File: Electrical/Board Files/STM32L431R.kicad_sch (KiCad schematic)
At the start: 11 parts

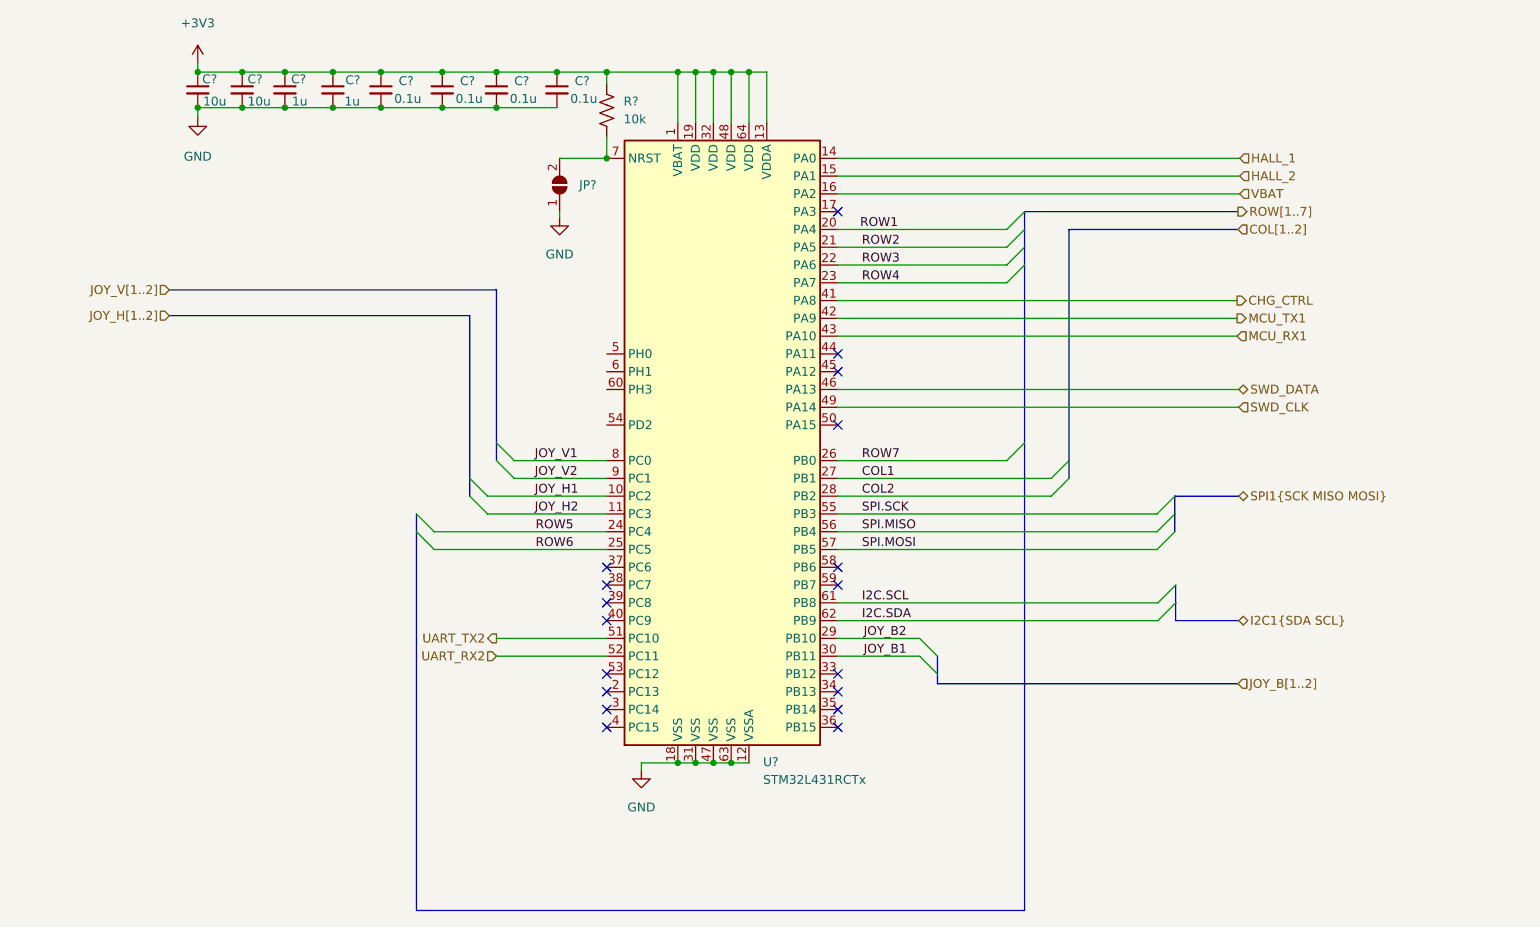
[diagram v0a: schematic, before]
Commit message: Added buzz and vibe, moved SPI, added 2 LEDs
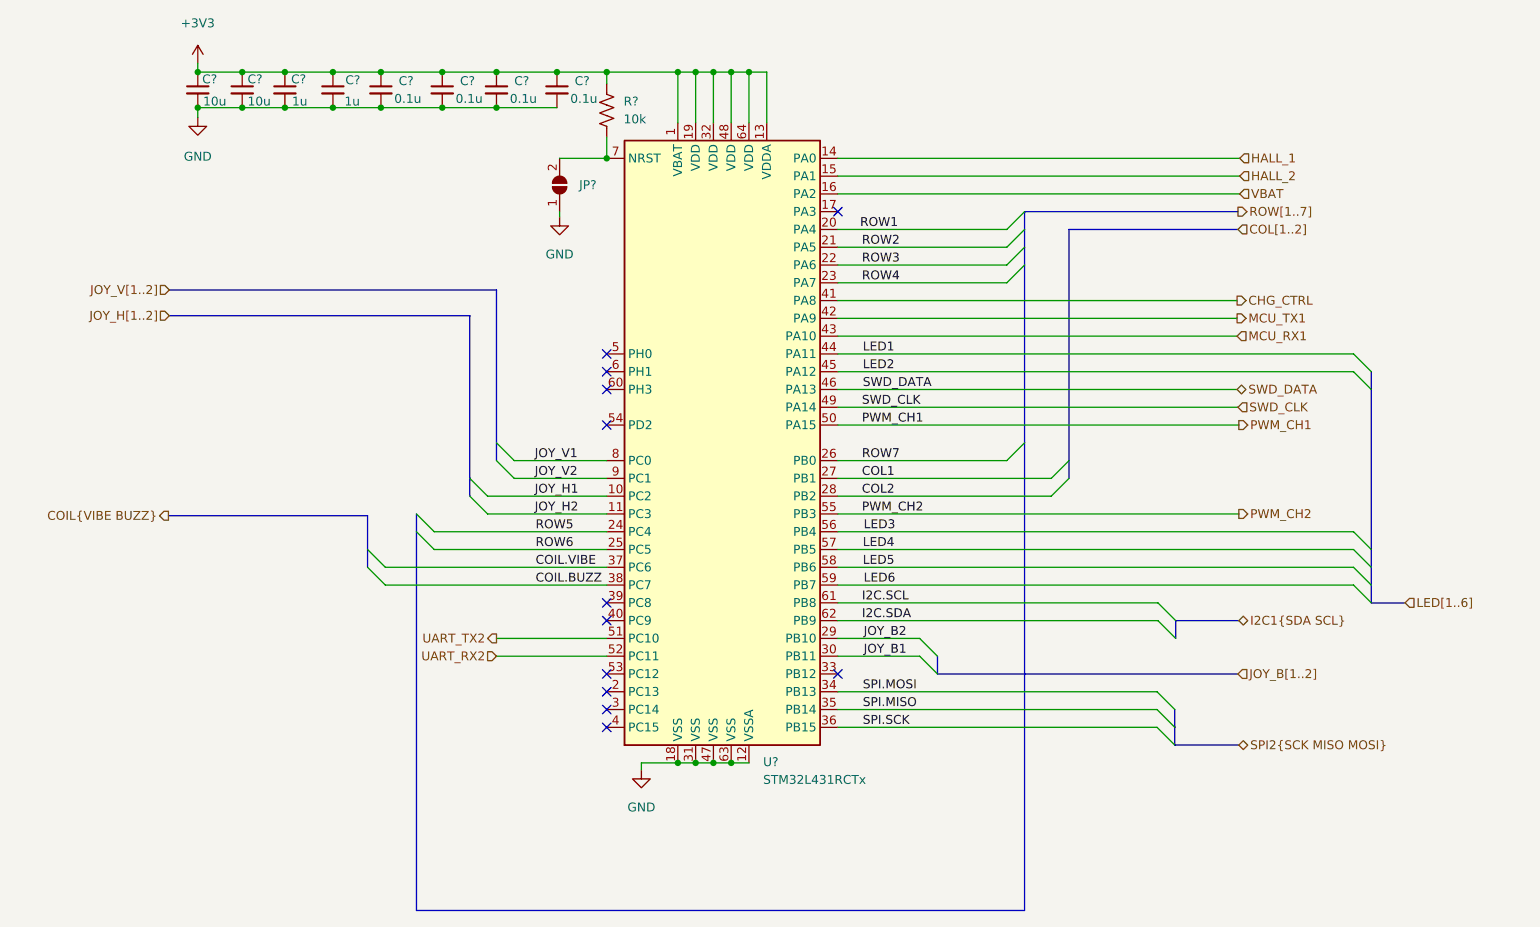
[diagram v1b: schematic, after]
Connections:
- net SPI.MISO: now also U?.35 (PB14); no longer U?.56 (PB4)
- net SPI.MOSI: now also U?.34 (PB13); no longer U?.57 (PB5)
- net SPI.SCK: now also U?.36 (PB15); no longer U?.55 (PB3)
- net COIL.VIBE: now reaches U?.37 (PC6)
- net COIL.BUZZ: now reaches U?.38 (PC7)
- net LED1: now reaches U?.44 (PA11)
- net LED2: now reaches U?.45 (PA12)
- net PWM_CH1: now reaches U?.50 (PA15)
- net LED5: now reaches U?.58 (PB6)
- net LED6: now reaches U?.59 (PB7)
- new net LED3: U?.56 (PB4)
- new net LED4: U?.57 (PB5)
- new net PWM_CH2: U?.55 (PB3)
- no-connect marks 18 -> 12

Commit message: Added Xbee libs and bus aliases
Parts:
- gave numbers to parts that had none: 11
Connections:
- net SWD.NRST: now reaches JP2.2 (B), R8.2, U3.7 (NRST)
- net HALL_1 renamed HALL1
- net HALL_2 renamed HALL2
- net MCU_RX1 renamed DEBUG_UART.TX
- net MCU_TX1 renamed DEBUG_UART.RX
- net SPI.MISO renamed SPI2.MISO
- net SPI.MOSI renamed SPI2.MOSI
- net SPI.SCK renamed SPI2.SCK
- net SWD_CLK renamed SWD.CLK
- net SWD_DATA renamed SWD.DATA
- net UART_RX2 renamed MCU_XB_UART.RX
- net UART_TX2 renamed MCU_XB_UART.TX
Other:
- title: (none) -> Robotics Controller
- moved on the sheet: C17, C18, C19, C20, C21, C22, C23, C24, JP2, R8, U3

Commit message: Added hall effect sensors
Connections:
- net DEBUG_UART.RX renamed DUART.RX
- net DEBUG_UART.TX renamed DUART.TX
- net I2C.SCL renamed I2C1.SCL
- net I2C.SDA renamed I2C1.SDA
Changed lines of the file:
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@@
     (effects (font (size 1.27 1.27)) (justify left bottom))
   )
-  (label "DEBUG_UART.RX" (at 162.306 74.422 0)
+  (label "DUART.RX" (at 162.306 74.422 0)
     (effects (font (size 1.27 1.27)) (justify left bottom))
   )
@@
     (effects (font (size 1.27 1.27)) (justify left bottom))
   )
-  (label "DEBUG_UART.TX" (at 162.306 76.962 0)
+  (label "DUART.TX" (at 162.306 76.962 0)
     (effects (font (size 1.27 1.27)) (justify left bottom))
   )
-  (label "I2C.SCL" (at 162.179 115.062 0)
+  (label "I2C1.SCL" (at 162.179 115.062 0)
     (effects (font (size 1.27 1.27)) (justify left bottom))
   )
@@
     (effects (font (size 1.27 1.27)) (justify left bottom))
   )
-  (label "I2C.SDA" (at 162.179 117.602 0)
+  (label "I2C1.SDA" (at 162.179 117.602 0)
     (effects (font (size 1.27 1.27)) (justify left bottom))
   )

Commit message: Updating title block fields and adding pdf schematic
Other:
- company: (none) -> Rockerbotics
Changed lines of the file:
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@@
   (title_block
     (title "Robotics Controller")
+    (date "2022-09-02")
     (rev "A")
+    (company "Rockerbotics")
   )
   (bus_alias "SWD" (members "DATA" "CLK" "NRST"))
